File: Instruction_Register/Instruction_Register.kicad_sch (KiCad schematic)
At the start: 25 parts, among them U1 74LS245, U2 74LS173, U3 74LS173

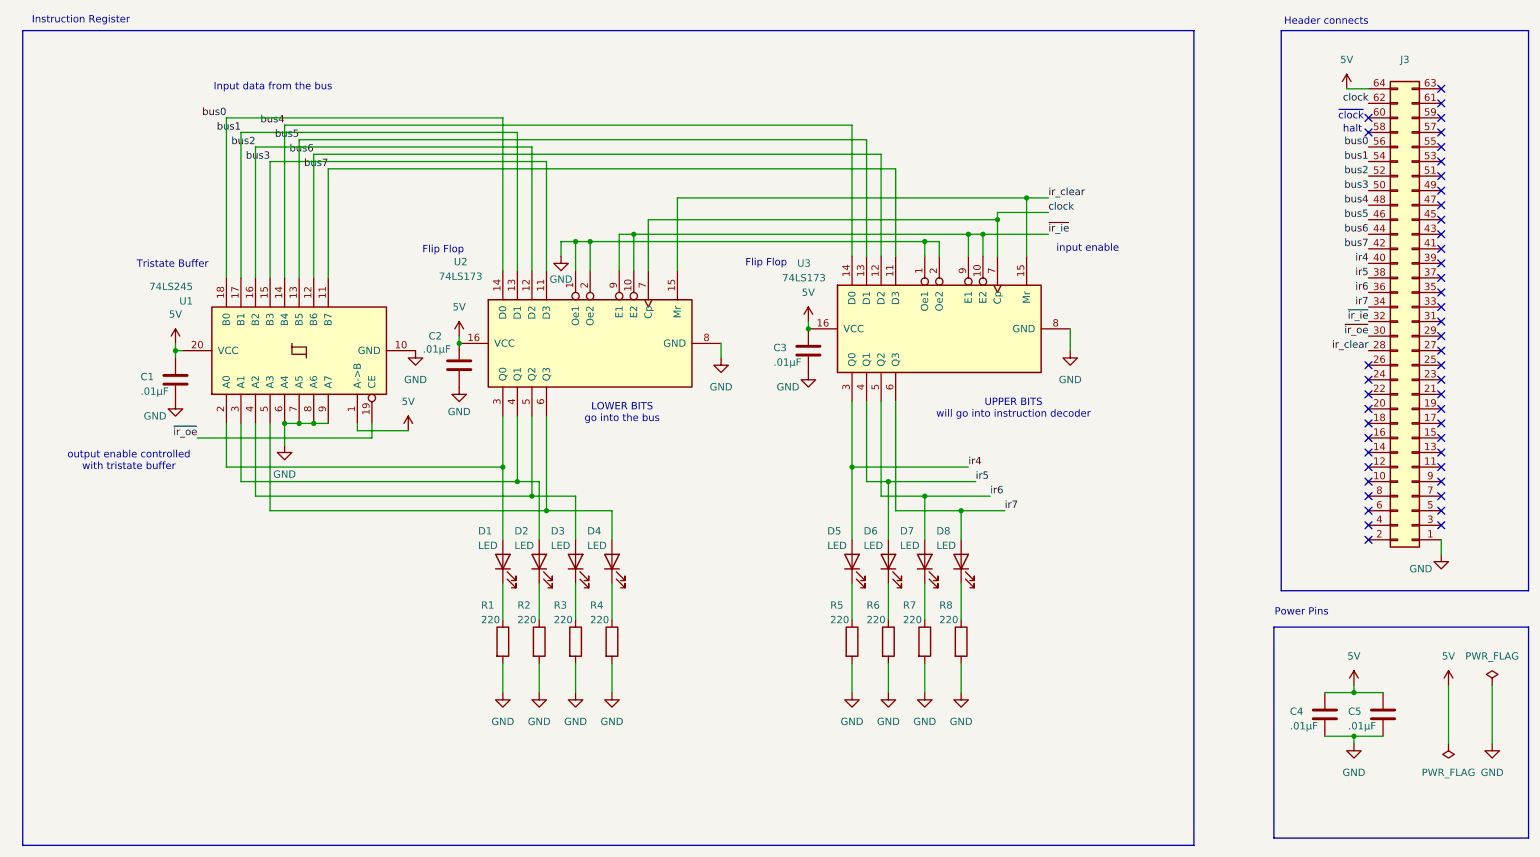
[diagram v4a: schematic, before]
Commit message: updated RAM, changed bus alignment in ALU, RAM, and registers
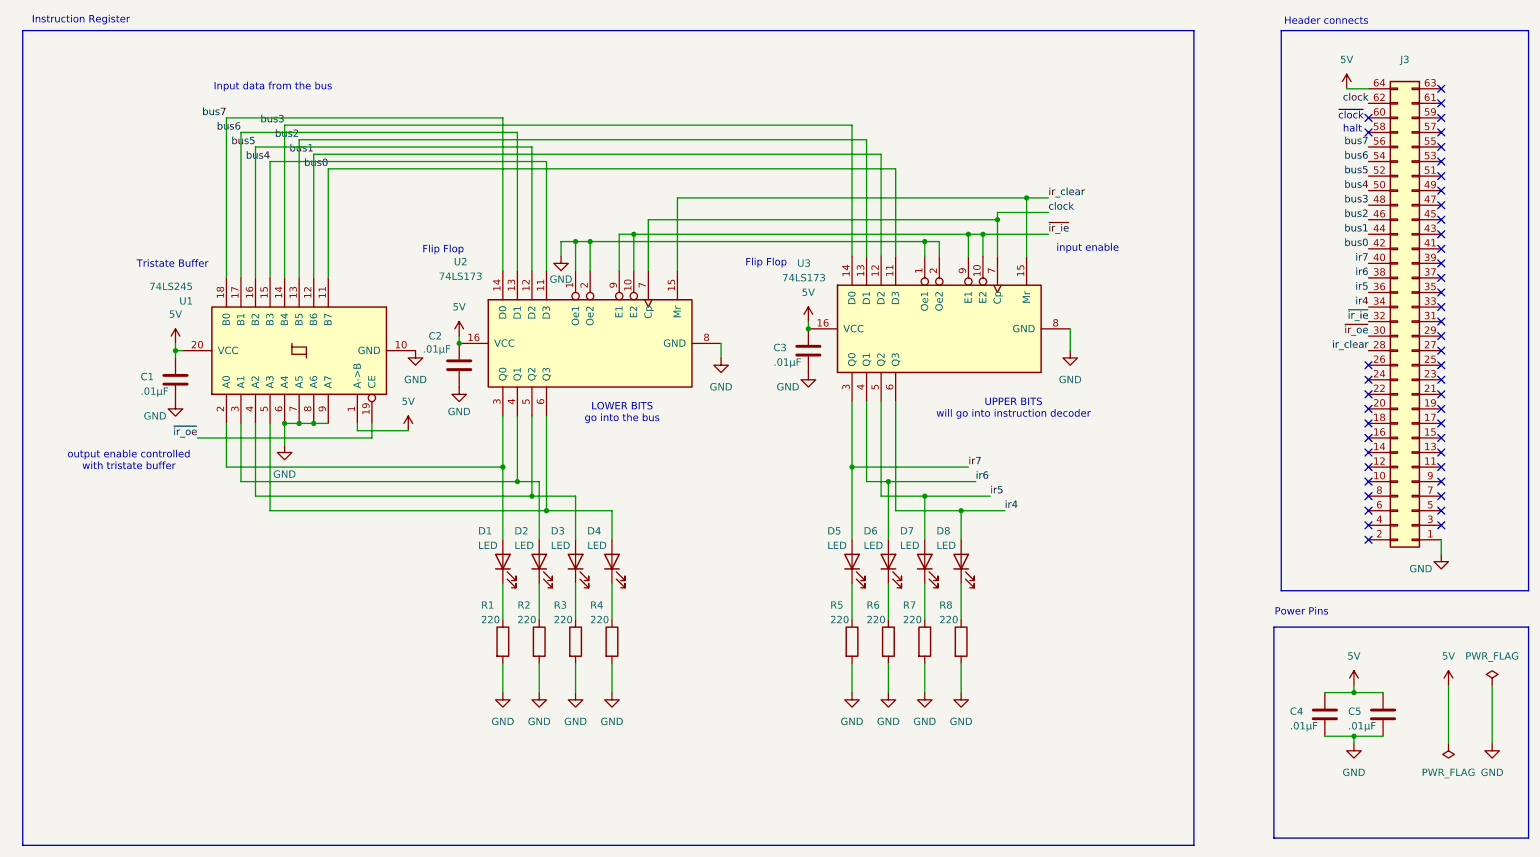
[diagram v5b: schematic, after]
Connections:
- net bus0: now also J3.42, U1.11 (B7), U3.11 (D3); no longer J3.56, U1.18 (B0), U2.14 (D0)
- net bus1: now also J3.44, U1.12 (B6), U3.12 (D2); no longer J3.54, U1.17 (B1), U2.13 (D1)
- net bus2: now also J3.46, U1.13 (B5), U3.13 (D1); no longer J3.52, U1.16 (B2), U2.12 (D2)
- net bus3: now also J3.48, U1.14 (B4), U3.14 (D0); no longer J3.50, U1.15 (B3), U2.11 (D3)
- net bus4: now also J3.50, U1.15 (B3), U2.11 (D3); no longer J3.48, U1.14 (B4), U3.14 (D0)
- net bus5: now also J3.52, U1.16 (B2), U2.12 (D2); no longer J3.46, U1.13 (B5), U3.13 (D1)
- net bus6: now also J3.54, U1.17 (B1), U2.13 (D1); no longer J3.44, U1.12 (B6), U3.12 (D2)
- net bus7: now also J3.56, U1.18 (B0), U2.14 (D0); no longer J3.42, U1.11 (B7), U3.11 (D3)
- net ir4: now also D8.2 (A), J3.34, U3.6 (Q3); no longer D5.2 (A), J3.40, U3.3 (Q0)
- net ir5: now also D7.2 (A), J3.36, U3.5 (Q2); no longer D6.2 (A), J3.38, U3.4 (Q1)
- net ir6: now also D6.2 (A), J3.38, U3.4 (Q1); no longer D7.2 (A), J3.36, U3.5 (Q2)
- net ir7: now also D5.2 (A), J3.40, U3.3 (Q0); no longer D8.2 (A), J3.34, U3.6 (Q3)
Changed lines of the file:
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@@
+	(wire
+		(pts
+			(xy 179.07 101.6) (xy 186.69 101.6)
+		)
+		(stroke
+			(width 0)
+			(type default)
+		)
+	)
 	(wire
 		(pts
@@
 		(pts
 			(xy 55.88 99.06) (xy 104.14 99.06)
-		)
-		(stroke
-			(width 0)
-			(type default)
-		)
-	)
-	(wire
-		(pts
-			(xy 186.69 101.6) (xy 179.07 101.6)
 		)
 		(stroke
@@
 		)
 	)
+	(label "bus5"
+		(at 250.19 43.18 180)
+		(effects
+			(font
+				(size 1.27 1.27)
+			)
+			(justify right bottom)
+		)
+	)
+	(label "bus4"
+		(at 250.19 45.72 180)
+		(effects
+			(font
+				(size 1.27 1.27)
+			)
+			(justify right bottom)
+		)
+	)
+	(label "bus0"
+		(at 68.58 41.91 180)
+		(effects
+			(font
+				(size 1.27 1.27)
+			)
+			(justify right bottom)
+		)
+	)
+	(label "bus2"
+		(at 250.19 50.8 180)
+		(effects
+			(font
+				(size 1.27 1.27)
+			)
+			(justify right bottom)
+		)
+	)
 	(label "bus3"
-		(at 250.19 45.72 180)
-		(effects
-			(font
-				(size 1.27 1.27)
-			)
-			(justify right bottom)
-		)
-	)
-	(label "bus6"
-		(at 250.19 53.34 180)
+		(at 60.96 34.29 180)
+		(effects
+			(font
+				(size 1.27 1.27)
+			)
+			(justify right bottom)
+		)
+	)
+	(label "ir7"
+		(at 250.19 58.42 180)
 		(effects
 			(font
@@
 	)
 	(label "bus1"
-		(at 250.19 40.64 180)
-		(effects
-			(font
-				(size 1.27 1.27)
-			)
-			(justify right bottom)
-		)
-	)
-	(label "bus4"
-		(at 250.19 48.26 180)
-		(effects
-			(font
-				(size 1.27 1.27)
-			)
-			(justify right bottom)
-		)
-	)
-	(label "ir4"
-		(at 180.34 93.98 0)
-		(effects
-			(font
-				(size 1.27 1.27)
-			)
-			(justify left bottom)
+		(at 66.04 39.37 180)
+		(effects
+			(font
+				(size 1.27 1.27)
+			)
+			(justify right bottom)
 		)
 	)
@@
 		)
 	)
+	(label "bus5"
+		(at 55.88 38.1 180)
+		(effects
+			(font
+				(size 1.27 1.27)
+			)
+			(justify right bottom)
+		)
+	)
 	(label "ir4"
-		(at 250.19 58.42 180)
-		(effects
-			(font
-				(size 1.27 1.27)
-			)
-			(justify right bottom)
-		)
-	)
-	(label "bus5"
-		(at 250.19 50.8 180)
-		(effects
-			(font
-				(size 1.27 1.27)
-			)
-			(justify right bottom)
-		)
-	)
-	(label "ir5"
-		(at 250.19 60.96 180)
-		(effects
-			(font
-				(size 1.27 1.27)
-			)
-			(justify right bottom)
+		(at 186.69 101.6 0)
+		(effects
+			(font
+				(size 1.27 1.27)
+			)
+			(justify left bottom)
 		)
 	)
@@
 		)
 	)
-	(label "bus0"
-		(at 50.8 33.02 180)
-		(effects
-			(font
-				(size 1.27 1.27)
-			)
-			(justify right bottom)
-		)
-	)
-	(label "bus7"
-		(at 250.19 55.88 180)
-		(effects
-			(font
-				(size 1.27 1.27)
-			)
-			(justify right bottom)
-		)
-	)
-	(label "bus0"
-		(at 250.19 38.1 180)
-		(effects
-			(font
-				(size 1.27 1.27)
-			)
-			(justify right bottom)
-		)
-	)
 	(label "~{ir_oe}"
 		(at 45.72 88.9 180)
@@
 		)
 	)
-	(label "ir6"
+	(label "bus2"
+		(at 63.5 36.83 180)
+		(effects
+			(font
+				(size 1.27 1.27)
+			)
+			(justify right bottom)
+		)
+	)
+	(label "bus3"
+		(at 250.19 48.26 180)
+		(effects
+			(font
+				(size 1.27 1.27)
+			)
+			(justify right bottom)
+		)
+	)
+	(label "ir5"
 		(at 184.15 99.06 0)
 		(effects
@@
 		)
 	)
-	(label "bus3"
-		(at 58.42 40.64 180)
-		(effects
-			(font
-				(size 1.27 1.27)
-			)
-			(justify right bottom)
-		)
-	)
-	(label "bus2"
-		(at 250.19 43.18 180)
+	(label "bus6"
+		(at 53.34 35.56 180)
 		(effects
 			(font
@@
 		)
 	)
-	(label "bus1"
-		(at 53.34 35.56 180)
+	(label "ir7"
+		(at 180.34 93.98 0)
+		(effects
+			(font
+				(size 1.27 1.27)
+			)
+			(justify left bottom)
+		)
+	)
+	(label "ir4"
+		(at 250.19 66.04 180)
 		(effects
 			(font
@@
 		)
 	)
+	(label "bus0"
+		(at 250.19 55.88 180)
+		(effects
+			(font
+				(size 1.27 1.27)
+			)
+			(justify right bottom)
+		)
+	)
+	(label "bus1"
+		(at 250.19 53.34 180)
+		(effects
+			(font
+				(size 1.27 1.27)
+			)
+			(justify right bottom)
+		)
+	)
 	(label "ir5"
+		(at 250.19 63.5 180)
+		(effects
+			(font
+				(size 1.27 1.27)
+			)
+			(justify right bottom)
+		)
+	)
+	(label "bus6"
+		(at 250.19 40.64 180)
+		(effects
+			(font
+				(size 1.27 1.27)
+			)
+			(justify right bottom)
+		)
+	)
+	(label "ir6"
+		(at 250.19 60.96 180)
+		(effects
+			(font
+				(size 1.27 1.27)
+			)
+			(justify right bottom)
+		)
+	)
+	(label "bus7"
+		(at 250.19 38.1 180)
+		(effects
+			(font
+				(size 1.27 1.27)
+			)
+			(justify right bottom)
+		)
+	)
+	(label "bus4"
+		(at 58.42 40.64 180)
+		(effects
+			(font
+				(size 1.27 1.27)
+			)
+			(justify right bottom)
+		)
+	)
+	(label "ir6"
 		(at 181.61 96.52 0)
 		(effects
@@
 			)
 			(justify left bottom)
-		)
-	)
-	(label "bus2"
-		(at 55.88 38.1 180)
-		(effects
-			(font
-				(size 1.27 1.27)
-			)
-			(justify right bottom)
-		)
-	)
-	(label "bus5"
-		(at 63.5 36.83 180)
-		(effects
-			(font
-				(size 1.27 1.27)
-			)
-			(justify right bottom)
-		)
-	)
-	(label "ir7"
-		(at 250.19 66.04 180)
-		(effects
-			(font
-				(size 1.27 1.27)
-			)
-			(justify right bottom)
-		)
-	)
-	(label "bus6"
-		(at 66.04 39.37 180)
-		(effects
-			(font
-				(size 1.27 1.27)
-			)
-			(justify right bottom)
-		)
-	)
-	(label "ir7"
-		(at 186.69 101.6 0)
-		(effects
-			(font
-				(size 1.27 1.27)
-			)
-			(justify left bottom)
-		)
-	)
-	(label "bus7"
-		(at 68.58 41.91 180)
-		(effects
-			(font
-				(size 1.27 1.27)
-			)
-			(justify right bottom)
 		)
 	)
@@
 		)
 	)
-	(label "ir6"
-		(at 250.19 63.5 180)
-		(effects
-			(font
-				(size 1.27 1.27)
-			)
-			(justify right bottom)
-		)
-	)
-	(label "bus4"
-		(at 60.96 34.29 180)
-		(effects
-			(font
+	(label "bus7"
+		(at 50.8 33.02 180)
+		(effects
+			(font

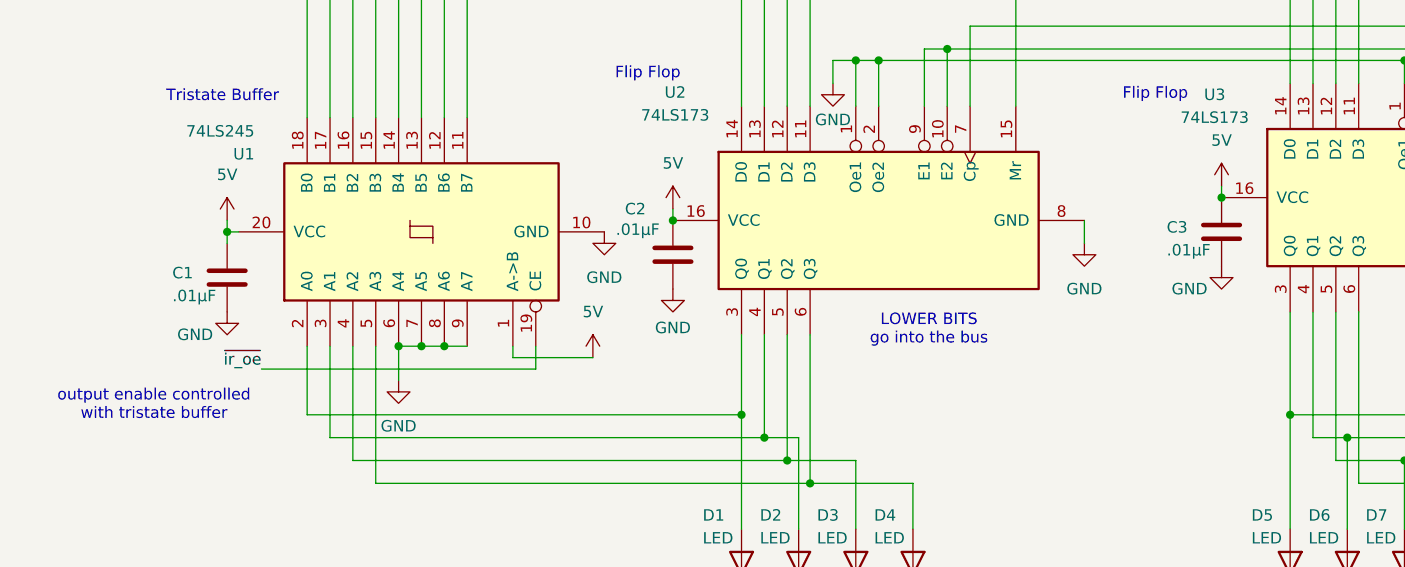
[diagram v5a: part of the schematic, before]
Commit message: fixed Ram register, fixed mar in ram.v, updated caps in alu, ram, and instruction register
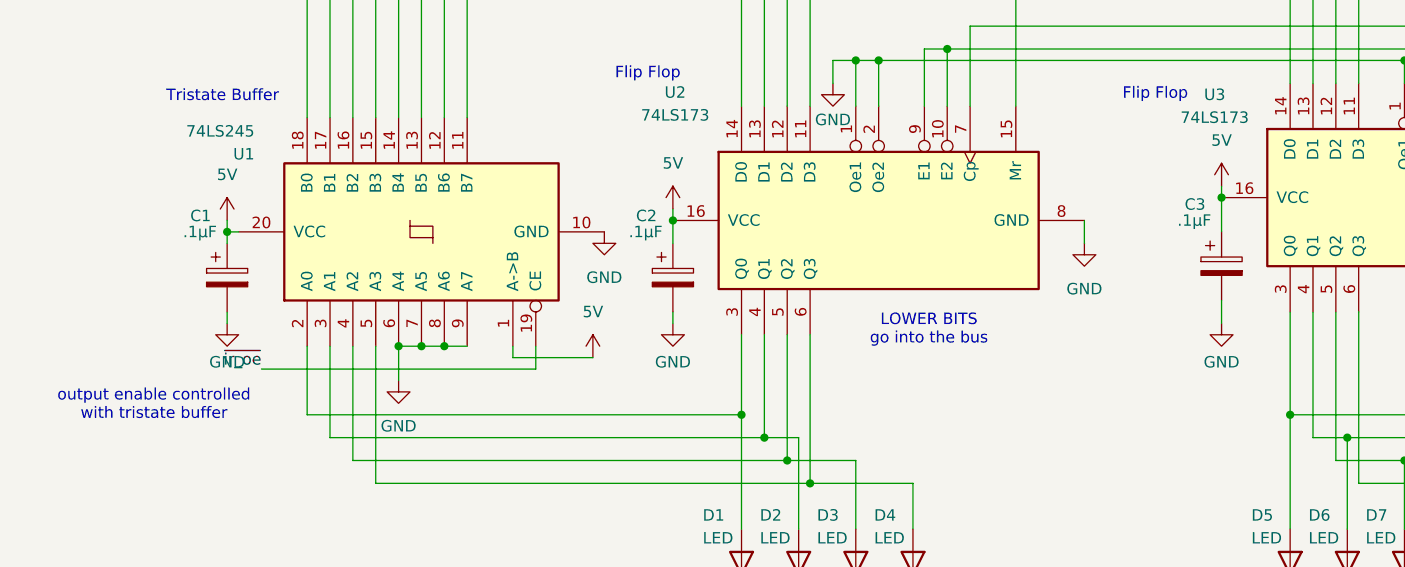
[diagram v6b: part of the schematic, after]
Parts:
- removed C1, C2, C3: .01µF, Capacitor_THT:C_Disc_D5.0mm_W2.5mm_P2.50mm, symbol Device:C
- added C1, C2, C3: .1µF, symbol Device:C_Polarized
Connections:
- net 5V: now also C1.1, C2.1, C3.1
- net GND: now also C1.2, C2.2, C3.2
